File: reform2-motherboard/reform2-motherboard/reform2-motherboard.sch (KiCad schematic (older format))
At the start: 38 parts, among them J15 Conn_01x33, J18 Conn_01x03_Male, J19 JTAG, J20 Conn_01x03_Male, SW3 SW_DIP_x01, SW6 SW_Push, U1 Nitrogen8M

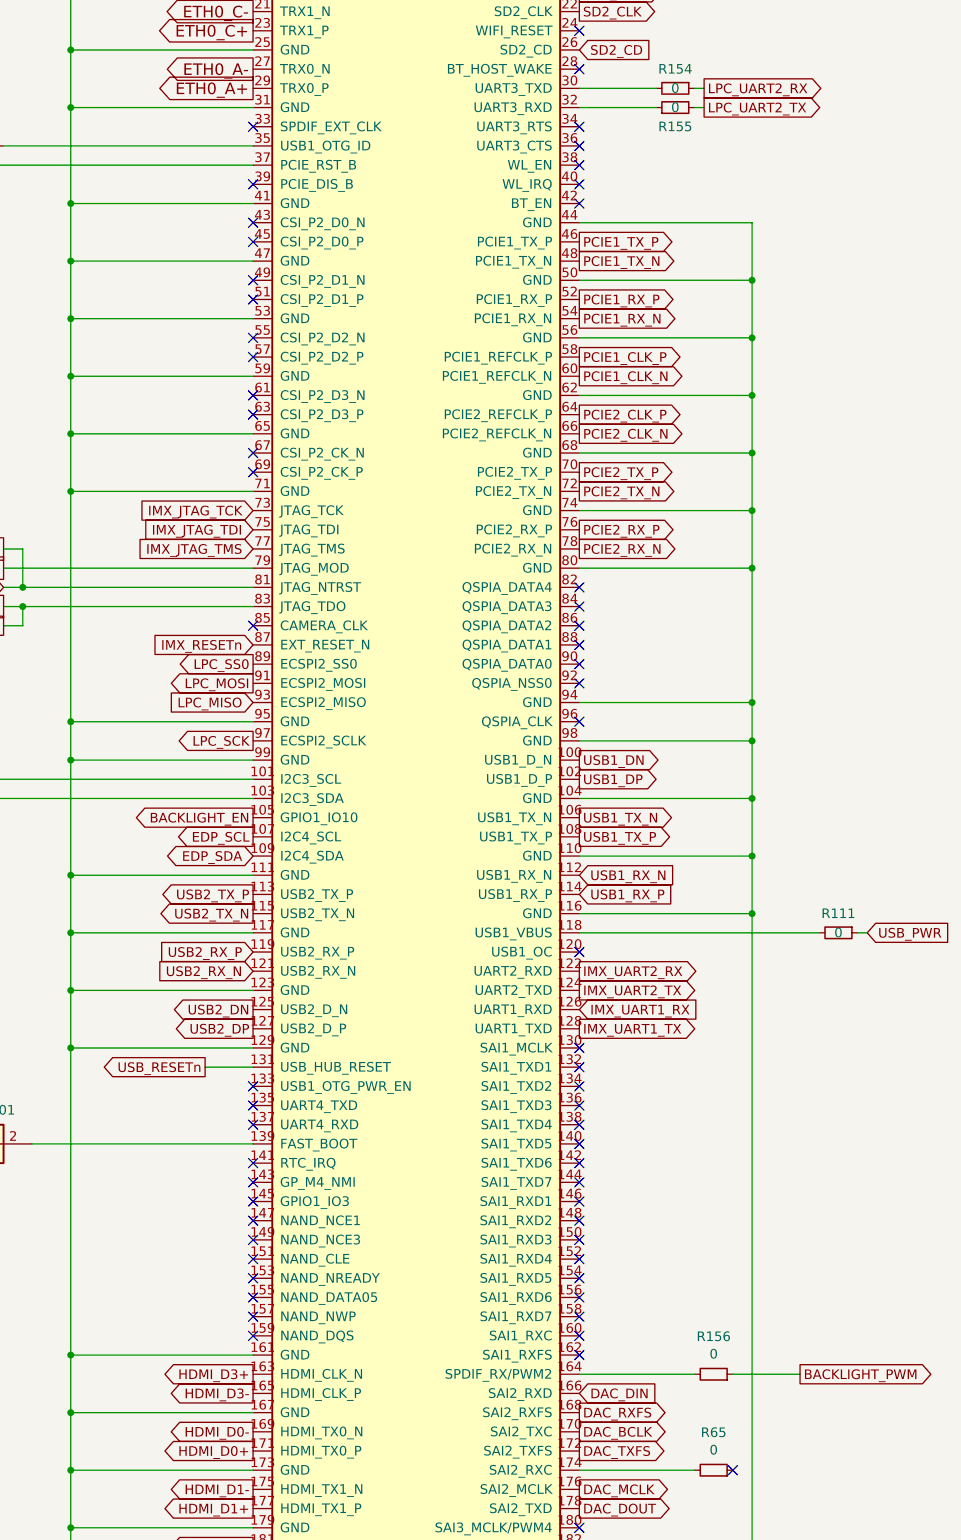
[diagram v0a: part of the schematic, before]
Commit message: reform2 motherboard: pinout and footprint checks completed; ERC checks fixed 100%
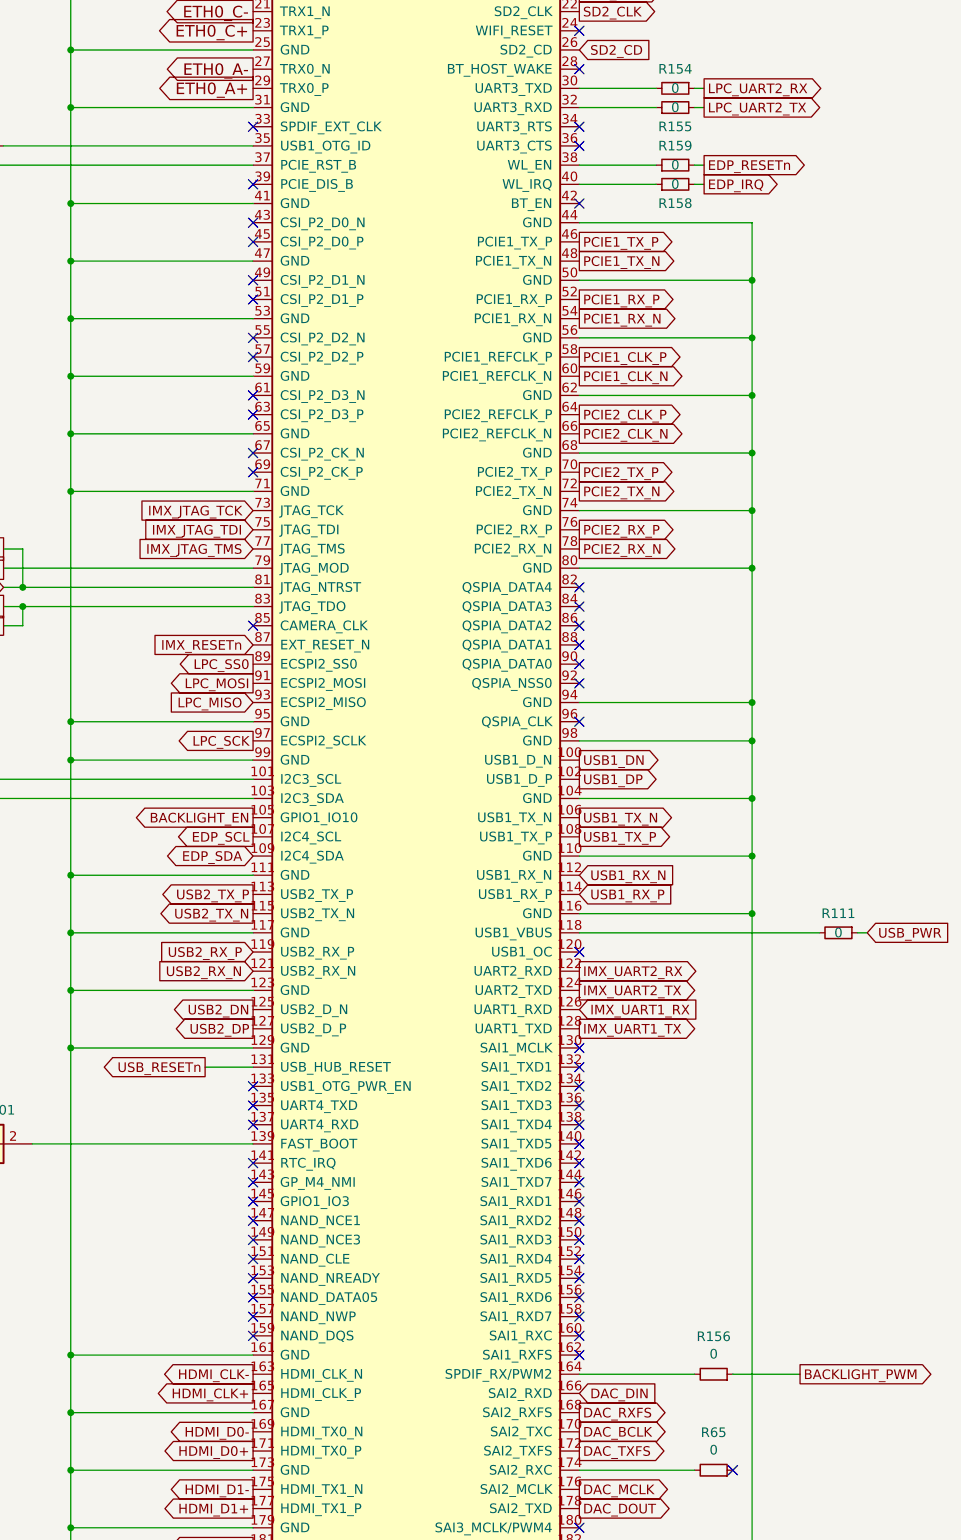
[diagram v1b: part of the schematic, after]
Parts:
- added R158, R159: 0, Resistor_SMD:R_0603_1608Metric, symbol Device:R_Small
- TP2, TP8: footprint TestPoint:TestPoint_Pad_1.0x1.0mm -> TestPoint:TestPoint_Pad_D1.0mm
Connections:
- net at U1.38 (WL_EN): now also R159.1
- net at U1.40 (WL_IRQ): now also R158.1
- net HDMI_D3+ renamed HDMI_CLK-
- net HDMI_D3- renamed HDMI_CLK+
- new net EDP_IRQ: R158.2
- new net EDP_RESETn: R159.2
- no-connect marks 90 -> 88
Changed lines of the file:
@@
 Text GLabel 10150 11750 0    50   Output ~ 0
 HDMI_D0-
+Text GLabel 10150 11550 0    50   Output ~ 0
+HDMI_CLK+
 Text GLabel 10150 11450 0    50   Output ~ 0
-HDMI_D3+
-Text GLabel 10150 11550 0    50   Output ~ 0
-HDMI_D3-
+HDMI_CLK-
 Text GLabel 10150 12450 0    50   Output ~ 0
 HDMI_D2+
@@
 F 0 "TP8" V 13204 3838 50  0000 L CNN
 F 1 "T_PMIC_ON_REQ" V 13295 3838 50  0000 L CNN
-F 2 "TestPoint:TestPoint_Pad_1.0x1.0mm" H 13450 3650 50  0001 C CNN
+F 2 "TestPoint:TestPoint_Pad_D1.0mm" H 13450 3650 50  0001 C CNN
 F 3 "~" H 13450 3650 50  0001 C CNN
 	1    13250 3650
@@
 F 0 "TP2" V 8804 5238 50  0000 L CNN
 F 1 "T_OTG" V 8895 5238 50  0000 L CNN
-F 2 "TestPoint:TestPoint_Pad_1.0x1.0mm" H 9050 5050 50  0001 C CNN
+F 2 "TestPoint:TestPoint_Pad_D1.0mm" H 9050 5050 50  0001 C CNN
 F 3 "~" H 9050 5050 50  0001 C CNN
 	1    8850 5050
@@
 NoConn ~ 11850 4650
 NoConn ~ 11850 5350
-NoConn ~ 11850 5250
-NoConn ~ 11850 5150
 NoConn ~ 10150 5250
 Wire Wire Line
@@
 Text GLabel 10150 7050 0    50   Input ~ 0
 IMX_JTAG_TDI
+Text GLabel 12500 5250 2    50   Output ~ 0
+EDP_IRQ
+$Comp
+L Device:R_Small R158
+U 1 1 636E4DF1
+P 12350 5250
+F 0 "R158" V 12250 5250 50  0000 C CNN
+F 1 "0" V 12350 5250 50  0000 C CNN
+F 2 "Resistor_SMD:R_0603_1608Metric" H 12350 5250 50  0001 C CNN
+F 3 "~" H 12350 5250 50  0001 C CNN
+	1    12350 5250
+	0    -1   -1   0
+$EndComp
+Wire Wire Line
+	12500 5250 12450 5250
+Wire Wire Line
+	11850 5250 12250 5250
+$Comp
+L Device:R_Small R159
+U 1 1 63FE6619
+P 12350 5150
+F 0 "R159" V 12450 5150 50  0000 C CNN
+F 1 "0" V 12350 5150 50  0000 C CNN
+F 2 "Resistor_SMD:R_0603_1608Metric" H 12350 5150 50  0001 C CNN
+F 3 "~" H 12350 5150 50  0001 C CNN
+	1    12350 5150
+	0    -1   -1   0
+$EndComp
+Text GLabel 12500 5150 2    50   Output ~ 0
+EDP_RESETn
+Wire Wire Line
+	12500 5150 12450 5150
+Wire Wire Line
+	11850 5150 12250 5150
 $EndSCHEMATC

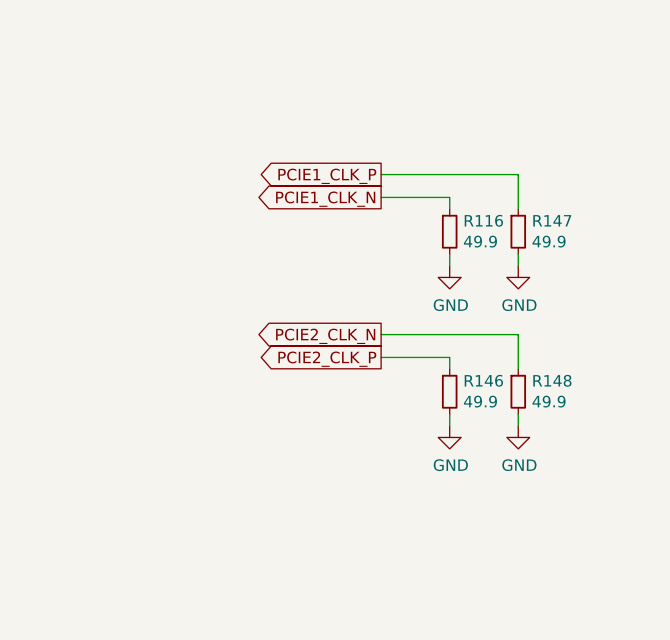
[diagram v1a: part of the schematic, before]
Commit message: reform2 motherboard: PCB DRC 100%
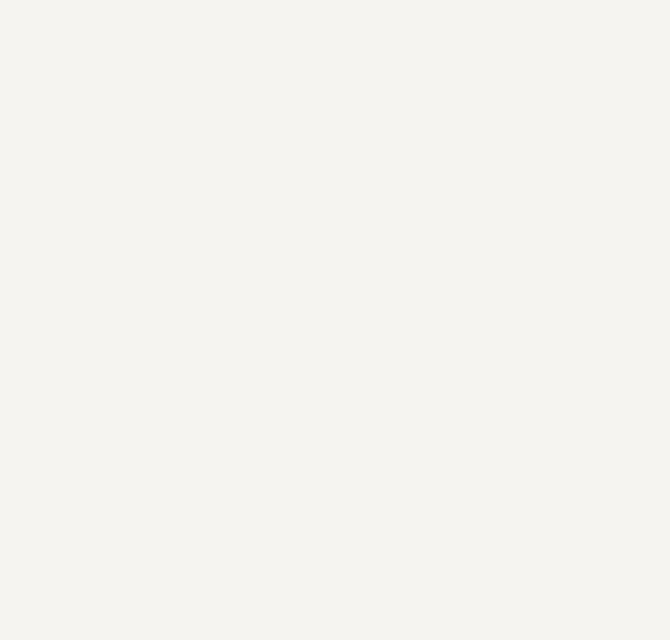
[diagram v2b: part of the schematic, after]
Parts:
- removed R116, R146, R147, R148: 49.9, Resistor_SMD:R_0603_1608Metric, symbol Device:R_Small
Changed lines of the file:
@@
 EndData
 $EndBitmap
-Text GLabel 20350 4950 0    50   Output ~ 0
-PCIE2_CLK_P
-Text GLabel 20350 4850 0    50   Output ~ 0
-PCIE2_CLK_N
-$Comp
-L Device:R_Small R146
-U 1 1 5E48CF70
-P 20650 5100
-F 0 "R146" H 20709 5146 50  0000 L CNN
-F 1 "49.9" H 20709 5055 50  0000 L CNN
-F 2 "Resistor_SMD:R_0603_1608Metric" H 20650 5100 50  0001 C CNN
-F 3 "~" H 20650 5100 50  0001 C CNN
-	1    20650 5100
-	1    0    0    -1
-$EndComp
-Wire Wire Line
-	20650 5000 20650 4950
-Wire Wire Line
-	20650 4950 20350 4950
-$Comp
-L power:GND #PWR0179
-U 1 1 5E4A242A
-P 20650 5250
-F 0 "#PWR0179" H 20650 5000 50  0001 C CNN
-F 1 "GND" H 20655 5077 50  0000 C CNN
-F 2 "" H 20650 5250 50  0001 C CNN
-F 3 "" H 20650 5250 50  0001 C CNN
-	1    20650 5250
-	1    0    0    -1
-$EndComp
-Wire Wire Line
-	20650 5250 20650 5200
-$Comp
-L Device:R_Small R148
-U 1 1 5E4B77EF
-P 20950 5100
-F 0 "R148" H 21009 5146 50  0000 L CNN
-F 1 "49.9" H 21009 5055 50  0000 L CNN
-F 2 "Resistor_SMD:R_0603_1608Metric" H 20950 5100 50  0001 C CNN
-F 3 "~" H 20950 5100 50  0001 C CNN
-	1    20950 5100
-	1    0    0    -1
-$EndComp
-Wire Wire Line
-	20350 4850 20950 4850
-Wire Wire Line
-	20950 4850 20950 5000
-$Comp
-L power:GND #PWR0192
-U 1 1 5E4CD0DC
-P 20950 5250
-F 0 "#PWR0192" H 20950 5000 50  0001 C CNN
-F 1 "GND" H 20955 5077 50  0000 C CNN
-F 2 "" H 20950 5250 50  0001 C CNN
-F 3 "" H 20950 5250 50  0001 C CNN
-	1    20950 5250
-	1    0    0    -1
-$EndComp
-Wire Wire Line
-	20950 5250 20950 5200
-Text GLabel 20350 4150 0    50   Output ~ 0
-PCIE1_CLK_P
-Text GLabel 20350 4250 0    50   Output ~ 0
-PCIE1_CLK_N
-$Comp
-L Device:R_Small R116
-U 1 1 5E50D670
-P 20650 4400
-F 0 "R116" H 20709 4446 50  0000 L CNN
-F 1 "49.9" H 20709 4355 50  0000 L CNN
-F 2 "Resistor_SMD:R_0603_1608Metric" H 20650 4400 50  0001 C CNN
-F 3 "~" H 20650 4400 50  0001 C CNN
-	1    20650 4400
-	1    0    0    -1
-$EndComp
-Wire Wire Line
-	20650 4300 20650 4250
-Wire Wire Line
-	20650 4250 20350 4250
-$Comp
-L power:GND #PWR0214
-U 1 1 5E50D67C
-P 20650 4550
-F 0 "#PWR0214" H 20650 4300 50  0001 C CNN
-F 1 "GND" H 20655 4377 50  0000 C CNN
-F 2 "" H 20650 4550 50  0001 C CNN
-F 3 "" H 20650 4550 50  0001 C CNN
-	1    20650 4550
-	1    0    0    -1
-$EndComp
-Wire Wire Line
-	20650 4550 20650 4500
-$Comp
-L Device:R_Small R147
-U 1 1 5E50D687
-P 20950 4400
-F 0 "R147" H 21009 4446 50  0000 L CNN
-F 1 "49.9" H 21009 4355 50  0000 L CNN
-F 2 "Resistor_SMD:R_0603_1608Metric" H 20950 4400 50  0001 C CNN
-F 3 "~" H 20950 4400 50  0001 C CNN
-	1    20950 4400
-	1    0    0    -1
-$EndComp
-Wire Wire Line
-	20350 4150 20950 4150
-Wire Wire Line
-	20950 4150 20950 4300
-$Comp
-L power:GND #PWR0215
-U 1 1 5E50D693
-P 20950 4550
-F 0 "#PWR0215" H 20950 4300 50  0001 C CNN
-F 1 "GND" H 20955 4377 50  0000 C CNN
-F 2 "" H 20950 4550 50  0001 C CNN
-F 3 "" H 20950 4550 50  0001 C CNN
-	1    20950 4550
-	1    0    0    -1
-$EndComp
-Wire Wire Line
-	20950 4550 20950 4500
 $Comp
 L power:+4V #PWR025

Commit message: reform2: motherboard final tweaks before first order
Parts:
- added H20, H21, H22, H23, H24, H25, H26, H27: MountingHole_Pad, MountingHole:MountingHole_2.2mm_M2_DIN965_Pad, symbol Mechanical:MountingHole_Pad
- added H4: WEEE, Symbol:WEEE-Logo_4.2x6mm_SilkScreen, symbol Mechanical:MountingHole
- added TP10: T_M4_NMI, TestPoint:TestPoint_Pad_D1.0mm, symbol Connector:TestPoint
- U1: Manufacturer (none) -> TE; Manufacturer_No (none) -> 1717254-1
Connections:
- net GND: now also H20.1, H21.1, H22.1, H23.1, H24.1, H25.1, H26.1, H27.1
- net at U1.143 (GP_M4_NMI): now also TP10.1
- no-connect marks 88 -> 87
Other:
- note added: "TE 1717254-1"
- note added: "or TE 1473005-1"
- moved on the sheet: H1, H10, H11, H12, H13, H14, H2, H3, H5, H6, H7, H8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

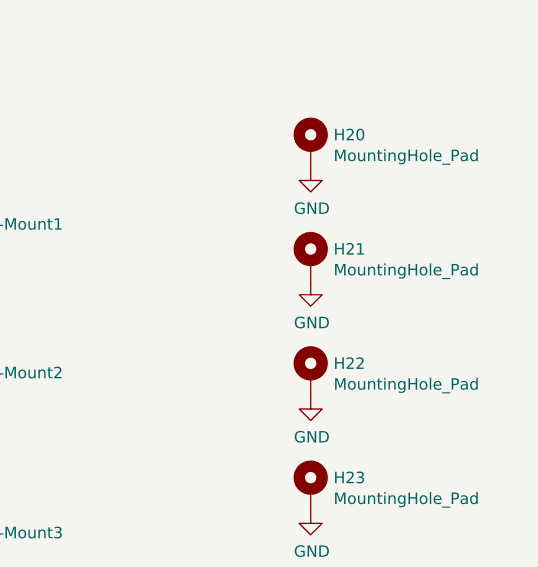
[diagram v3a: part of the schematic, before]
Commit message: reform2: fixed last minute EDP lane polarity error; added EDP dupont breakout
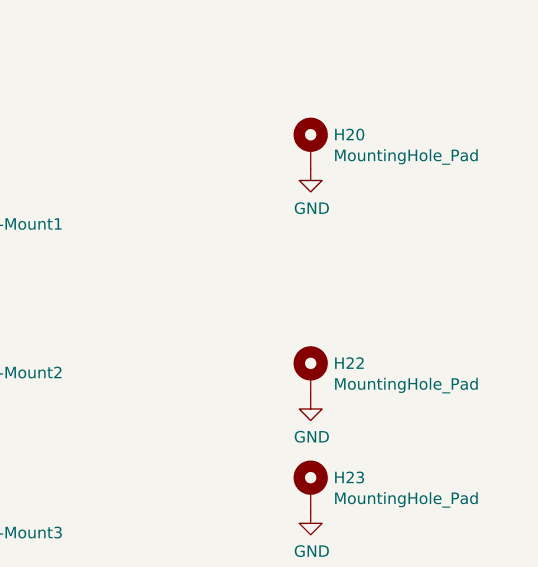
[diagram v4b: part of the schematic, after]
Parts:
- removed H21: MountingHole_Pad, MountingHole:MountingHole_2.2mm_M2_DIN965_Pad, symbol Mechanical:MountingHole_Pad
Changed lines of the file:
@@
-$EndComp
-$Comp
-L power:GND #PWR0192
-U 1 1 5D3A8AFD
-P 18000 7900
-F 0 "#PWR0192" H 18000 7650 50  0001 C CNN
-F 1 "GND" H 18005 7727 50  0000 C CNN
-F 2 "" H 18000 7900 50  0001 C CNN
-F 3 "" H 18000 7900 50  0001 C CNN
-	1    18000 7900
-	1    0    0    -1
-$EndComp
-$Comp
-L Mechanical:MountingHole_Pad H21
-U 1 1 5D3A8B07
-P 18000 7800
-F 0 "H21" H 18100 7849 50  0000 L CNN
-F 1 "MountingHole_Pad" H 18100 7758 50  0000 L CNN
-F 2 "MountingHole:MountingHole_2.2mm_M2_DIN965_Pad" H 18000 7800 50  0001 C CNN
-F 3 "~" H 18000 7800 50  0001 C CNN
-	1    18000 7800
-	1    0    0    -1
 $EndComp
 $Comp

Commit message: reform2 motherboard: add part numbers
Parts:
- J15: Manufacturer (none) -> Hirose; Manufacturer_No (none) -> FH12-33S-0.5SH(55)
- J18, J20: Manufacturer TE -> Wurth; Manufacturer_No 826936-3 -> 61300311121
- J19: Manufacturer (none) -> Molex; Manufacturer_No (none) -> 87914-2016
- R111, R153, R154, R155, R156, R158, R159, R65: Manufacturer (none) -> Vishay Dale; Manufacturer_No (none) -> CRCW06030000Z0EAC
- R149: Manufacturer_No CRCW060310K0JNEAC -> CRCW06030000Z0EAC
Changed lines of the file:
@@
 F 2 "Resistor_SMD:R_0603_1608Metric" H 10900 5350 50  0001 C CNN
 F 3 "~" H 10900 5350 50  0001 C CNN
+F 4 "Vishay Dale" H 10900 5350 50  0001 C CNN "Manufacturer"
+F 5 "CRCW06030000Z0EAC" H 10900 5350 50  0001 C CNN "Manufacturer_No"
 	1    10900 5350
 	0    -1   -1   0
@@
 F 2 "Resistor_SMD:R_0603_1608Metric" H 10900 5450 50  0001 C CNN
 F 3 "~" H 10900 5450 50  0001 C CNN
+F 4 "Vishay Dale" H 10900 5450 50  0001 C CNN "Manufacturer"
+F 5 "CRCW06030000Z0EAC" H 10900 5450 50  0001 C CNN "Manufacturer_No"
 	1    10900 5450
 	0    -1   -1   0
@@
 F 2 "Resistor_SMD:R_0603_1608Metric" H 10900 5050 50  0001 C CNN
 F 3 "~" H 10900 5050 50  0001 C CNN
+F 4 "Vishay Dale" H 10900 5050 50  0001 C CNN "Manufacturer"
+F 5 "CRCW06030000Z0EAC" H 10900 5050 50  0001 C CNN "Manufacturer_No"
 	1    10900 5050
 	0    -1   -1   0
@@
 F 2 "Resistor_SMD:R_0603_1608Metric" H 10900 4950 50  0001 C CNN
 F 3 "~" H 10900 4950 50  0001 C CNN
+F 4 "Vishay Dale" H 10900 4950 50  0001 C CNN "Manufacturer"
+F 5 "CRCW06030000Z0EAC" H 10900 4950 50  0001 C CNN "Manufacturer_No"
 	1    10900 4950
 	0    1    1    0
@@
 F 2 "Resistor_SMD:R_0603_1608Metric" H 11100 11650 50  0001 C CNN
 F 3 "~" H 11100 11650 50  0001 C CNN
+F 4 "Vishay Dale" H 11100 11650 50  0001 C CNN "Manufacturer"
+F 5 "CRCW06030000Z0EAC" H 11100 11650 50  0001 C CNN "Manufacturer_No"
 	1    11100 11650
 	0    1    -1   0
@@
 F 2 "Resistor_SMD:R_0603_1608Metric" H 6700 5350 50  0001 C CNN
 F 3 "~" H 6700 5350 50  0001 C CNN
+F 4 "Vishay Dale" H 6700 5350 50  0001 C CNN "Manufacturer"
+F 5 "CRCW06030000Z0EAC" H 6700 5350 50  0001 C CNN "Manufacturer_No"
 	1    6700 5350
 	0    1    1    0
@@
 F 2 "Resistor_SMD:R_0603_1608Metric" H 11100 12150 50  0001 C CNN
 F 3 "~" H 11100 12150 50  0001 C CNN
+F 4 "Vishay Dale" H 11100 12150 50  0001 C CNN "Manufacturer"
+F 5 "CRCW06030000Z0EAC" H 11100 12150 50  0001 C CNN "Manufacturer_No"
 	1    11100 12150
 	0    1    -1   0
@@
 F 2 "Connector_FFC-FPC:Hirose_FH12-33S-0.5SH_1x33-1MP_P0.50mm_Horizontal" H 3450 8350 50  0001 C CNN
 F 3 "~" H 3450 8350 50  0001 C CNN
+F 4 "Hirose" H 3450 8350 50  0001 C CNN "Manufacturer"
+F 5 "FH12-33S-0.5SH(55)" H 3450 8350 50  0001 C CNN "Manufacturer_No"
 	1    3450 8350
 	-1   0    0    1
@@
 F 3 "~" H 15850 5050 50  0001 C CNN
 F 4 "Vishay Dale" H 15850 5050 50  0001 C CNN "Manufacturer"
-F 5 "CRCW060310K0JNEAC" H 15850 5050 50  0001 C CNN "Manufacturer_No"
+F 5 "CRCW06030000Z0EAC" H 15850 5050 50  0001 C CNN "Manufacturer_No"
 	1    15850 5050
 	0    1    1    0
@@
 F 2 "Connector_PinHeader_2.54mm:PinHeader_2x10_P2.54mm_Vertical" H 16200 5350 50  0001 C CNN
 F 3 "~" H 16200 5350 50  0001 C CNN
+F 4 "Molex" H 16200 5350 50  0001 C CNN "Manufacturer"
+F 5 "87914-2016" H 16200 5350 50  0001 C CNN "Manufacturer_No"
 	1    16200 5350
 	1    0    0    -1
@@
 F 2 "Resistor_SMD:R_0603_1608Metric" H 11750 9350 50  0001 C CNN
 F 3 "~" H 11750 9350 50  0001 C CNN
+F 4 "Vishay Dale" H 11750 9350 50  0001 C CNN "Manufacturer"
+F 5 "CRCW06030000Z0EAC" H 11750 9350 50  0001 C CNN "Manufacturer_No"
 	1    11750 9350
 	0    1    1    0
@@
 F 2 "Connector_PinHeader_2.54mm:PinHeader_1x03_P2.54mm_Vertical" H 16000 3200 50  0001 C CNN
 F 3 "~" H 16000 3200 50  0001 C CNN
-F 4 "TE" H 16000 3200 50  0001 C CNN "Manufacturer"
-F 5 "826936-3" H 16000 3200 50  0001 C CNN "Manufacturer_No"
+F 4 "Wurth" H 16000 3200 50  0001 C CNN "Manufacturer"
+F 5 "61300311121" H 16000 3200 50  0001 C CNN "Manufacturer_No"
 	1    16000 3200
 	1    0    0    -1
@@
 F 2 "Connector_PinHeader_2.54mm:PinHeader_1x03_P2.54mm_Vertical" H 14650 3200 50  0001 C CNN
 F 3 "~" H 14650 3200 50  0001 C CNN
-F 4 "TE" H 14650 3200 50  0001 C CNN "Manufacturer"
-F 5 "826936-3" H 14650 3200 50  0001 C CNN "Manufacturer_No"
+F 4 "Wurth" H 14650 3200 50  0001 C CNN "Manufacturer"
+F 5 "61300311121" H 14650 3200 50  0001 C CNN "Manufacturer_No"
 	1    14650 3200
 	1    0    0    -1
